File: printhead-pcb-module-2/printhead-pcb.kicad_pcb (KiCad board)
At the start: 2 copper layers, 136.4 x 35.3 mm, 55 parts, among them J1 Power, J13 Steckverbinder_Male_1, J14 Steckverbinder_Male_2, J15 Steckverbinder_Female_2, J2 Fan_12/5V_Regelung, J3 DATA, J4 FAN0, J5 FAN1, J6 FAN2, J7 FAN4, Q1 DTC143E, Q2 DTC143E, Q4 DTC143E, Q5 DTC143E, U1 PCA9615DP, U2 EMC2302-2-AIZL-TR, U5 PCA9536D, U6 AP7361C-33E

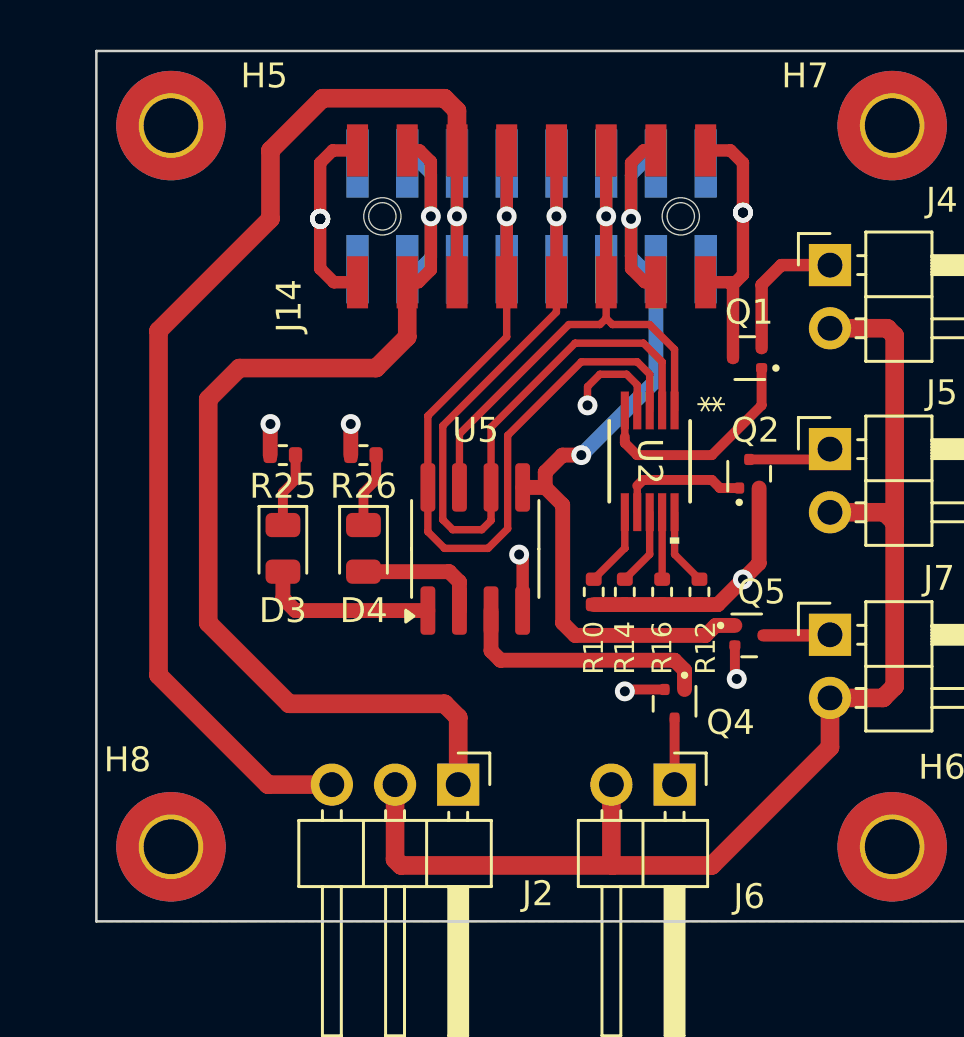
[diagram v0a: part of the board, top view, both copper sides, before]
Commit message: added documentation, fixed isolated copper fill warnings
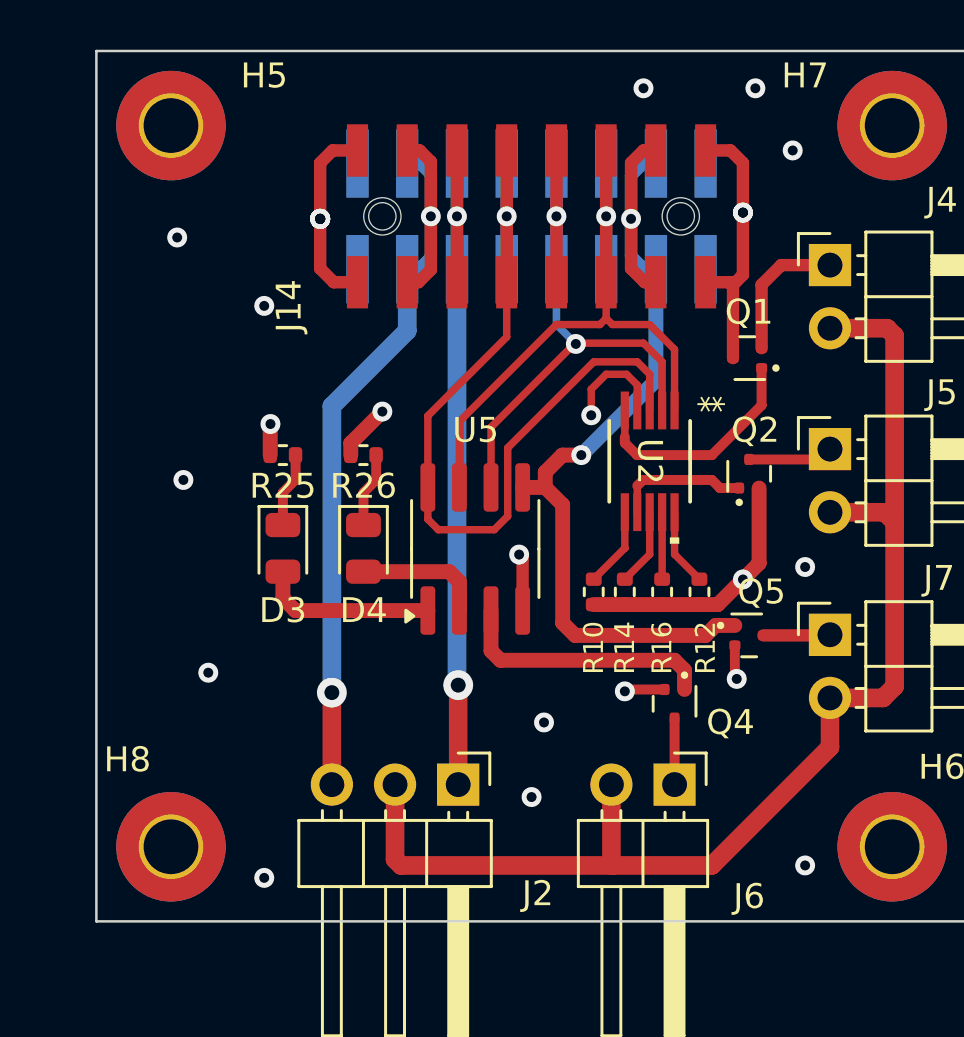
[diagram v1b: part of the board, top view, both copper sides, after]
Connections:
- J2 pad 1: +12V -> +5V
- J2 pad 3: +5V -> +12V
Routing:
- net +5V: track 129.4 -> 108.2 mm, vias 1 -> 2
- net +12V: track 78.4 -> 65.9 mm, vias 1 -> 2
- net SCL: track 60.3 -> 48.6 mm, vias 1 -> 2
- net +3V3: track 49.8 -> 48.3 mm
- net GND: track 41.0 -> 42.2 mm, vias 14 -> 26
- removed copper zone on F.Cu, net SCL

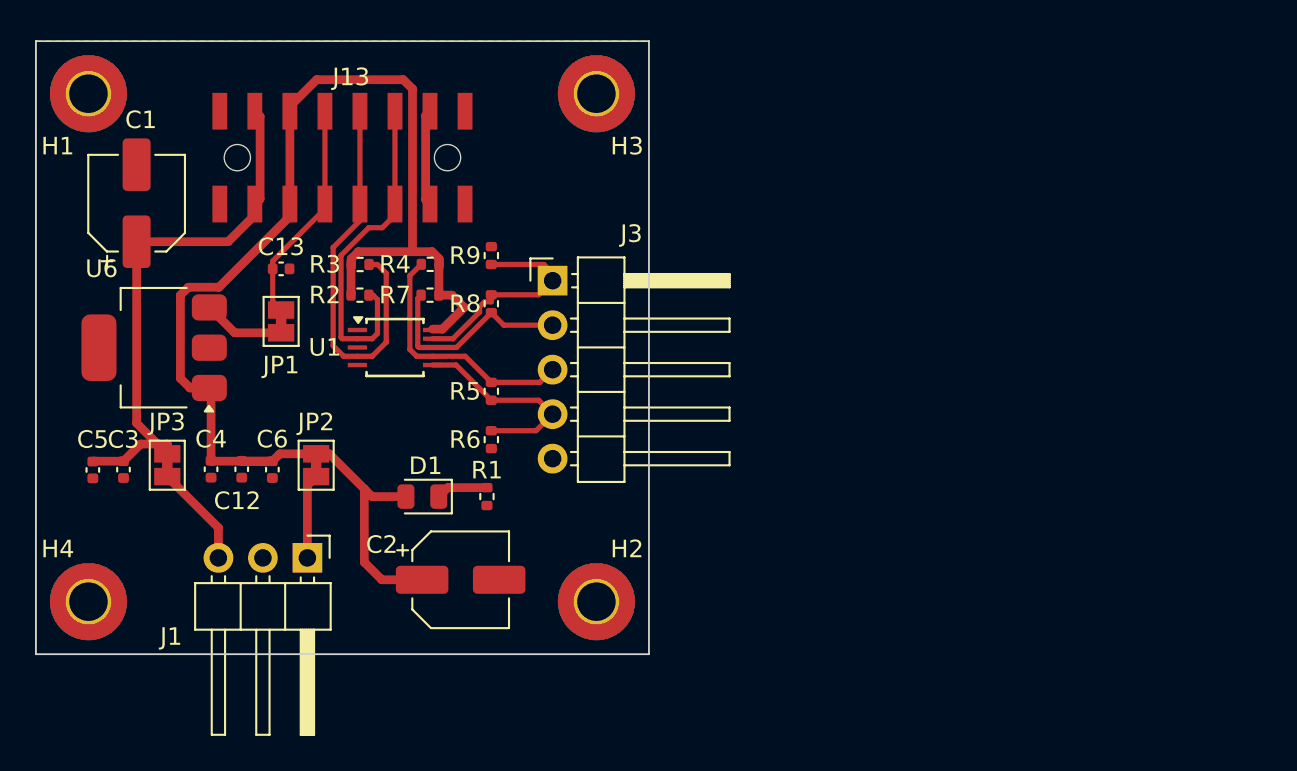
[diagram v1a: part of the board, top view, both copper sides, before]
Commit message: added first module into projet of second module
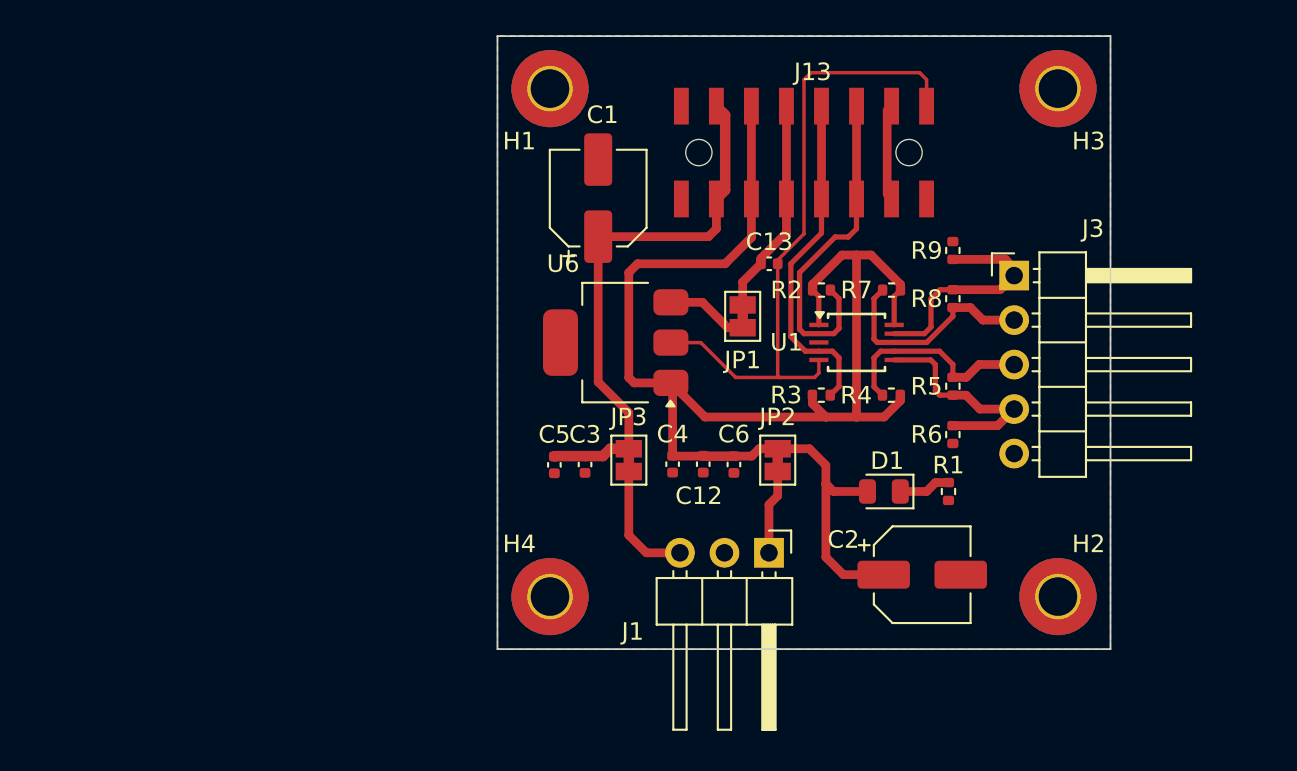
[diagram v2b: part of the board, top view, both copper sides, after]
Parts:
- moved C13 27.9 mm to (90.4, 113.0)
- moved R4 27.4 mm to (97.4, 120.5)
- moved R3 27.4 mm to (93.4, 120.5)
- moved C1 26.4 mm to (80.7, 109.3)
- moved C12 26.4 mm to (86.7, 124.5)
- moved C2 26.4 mm to (99.2, 130.8)
- moved C3 26.4 mm to (79.9, 124.5)
- moved C4 26.4 mm to (84.9, 124.5)
- moved C5 26.4 mm to (78.2, 124.5)
- moved C6 26.4 mm to (88.4, 124.5)
- moved D1 26.4 mm to (97.0, 126.0)
- moved H1 26.4 mm to (77.9, 103.0)
- moved H2 26.4 mm to (106.9, 132.0)
- moved H3 26.4 mm to (106.9, 103.0)
- moved H4 26.4 mm to (77.9, 132.0)
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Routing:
- net GND: track 42.2 -> 78.8 mm
- net +5V: track 108.2 -> 117.7 mm
- net SCL: track 48.6 -> 45.3 mm
- net DSCLP: track 14.4 -> 11.8 mm
- net Net-(J1-Pin_3): track 5.85 -> 6.97 mm
- net DSCLM: track 11.9 -> 12.8 mm
- net DSDAP: track 11.8 -> 12.5 mm
- net DSDAM: track 12.8 -> 13.3 mm
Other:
- board size 136.4 x 35.3 mm -> 110.1 x 35 mm

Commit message: finished third module
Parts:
- added C10: 0.1µF, Capacitor_SMD:C_0402_1005Metric, F.Cu at (175.0, 68.0)
- added C11: 0.1µF, Capacitor_SMD:C_0402_1005Metric, F.Cu at (175.0, 62.0)
- added C7: 0.1µF, Capacitor_SMD:C_0402_1005Metric, F.Cu at (172.5, 75.0)
- added C8: 0.1µF, Capacitor_SMD:C_0402_1005Metric, F.Cu at (170.3, 51.8)
- added C9: 0.1µF, Capacitor_SMD:C_0402_1005Metric, F.Cu at (175.0, 74.0)
- added D2: BLUE, LED_SMD:LED_0805_2012Metric, F.Cu at (167.0, 74.3)
- added H10: MountHole, MountingHole:MountingHole_2.2mm_M2_Pad_TopBottom, F.Cu at (182.0, 82.0)
- added H11: MountHole, MountingHole:MountingHole_2.2mm_M2_Pad_TopBottom, F.Cu at (182.0, 53.0)
- added H12: MountHole, MountingHole:MountingHole_2.2mm_M2_Pad_TopBottom, F.Cu at (153.0, 82.0)
- added H9: MountHole, MountingHole:MountingHole_2.2mm_M2_Pad_TopBottom, F.Cu at (153.0, 53.0)
- added J10: T2, Connector_PinHeader_2.54mm:PinHeader_1x02_P2.54mm_Horizontal, F.Cu at (179.5, 66.0)
- added J11: T3, Connector_PinHeader_2.54mm:PinHeader_1x02_P2.54mm_Horizontal, F.Cu at (179.5, 58.6)
- added J12: Breakout_Board_ADXL345, Connector_PinHeader_2.54mm:PinHeader_1x04_P2.54mm_Horizontal, F.Cu at (166.7, 79.5)
- added J16: Steckverbinder_Male_3, CustomFotLibByJan:BF100-16-A-D-1-0640-L-C, F.Cu at (160.5, 59.3)
- added J17: Steckverbinder_Female_3, CustomFotLibByJan:BF030-16A-B1-0360-0277-0600-LB, B.Cu at (174.5, 58.8)
- added J8: T0, Connector_PinHeader_2.54mm:PinHeader_1x02_P2.54mm_Horizontal, F.Cu at (175.5, 79.5)
- added J9: T1, Connector_PinHeader_2.54mm:PinHeader_1x02_P2.54mm_Horizontal, F.Cu at (179.5, 73.5)
- added R18: 4k7, Resistor_SMD:R_0402_1005Metric, F.Cu at (170.5, 75.0)
- added R19: 4k7, Resistor_SMD:R_0402_1005Metric, F.Cu at (175.0, 76.0)
- added R20: 330, Resistor_SMD:R_0402_1005Metric, F.Cu at (164.5, 75.1)
- added R21: 4k7, Resistor_SMD:R_0402_1005Metric, F.Cu at (175.0, 70.0)
- added R22: 4k7, Resistor_SMD:R_0402_1005Metric, F.Cu at (175.0, 64.0)
- added U4: ADS1015IDGS, Package_SO:TSSOP-10_3x3mm_P0.5mm, F.Cu at (168.8, 68.8)
- moved D4 70.7 mm to (110.7, 70.0)
- moved J2 70.7 mm to (114.5, 79.5)
- moved R26 70.7 mm to (110.7, 66.2)
- moved U5 70.7 mm to (115.2, 70.0)
- moved D3 70.7 mm to (107.5, 70.0)
- moved H5 70.7 mm to (103.0, 53.0)
- moved H6 70.7 mm to (132.0, 82.0)
- moved H7 70.7 mm to (132.0, 53.0)
- moved H8 70.7 mm to (103.0, 82.0)
- moved J14 70.7 mm to (110.5, 59.3)
- moved J15 70.7 mm to (124.5, 58.8)
- moved J4 70.7 mm to (129.5, 58.6)
- moved J5 70.7 mm to (129.5, 66.0)
- moved J6 70.7 mm to (123.2, 79.5)
- moved J7 70.7 mm to (129.5, 73.5)
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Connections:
- net +3V3 renamed AREF
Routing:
- net AREF: track 47.9 -> 105.2 mm, vias 1 -> 4
- net GND: track 78.8 -> 126.6 mm, vias 26 -> 28
- net SCL: track 45.3 -> 79.0 mm, vias 2 -> 3
- net SDA: track 46.4 -> 79.8 mm, vias 1 -> 2
- net +5V: track 117.7 -> 148.3 mm, vias 2 -> 4
- net ADC3: track 0.00 -> 12.7 mm
- net IO3: track 42.5 -> 54.9 mm, vias 2 -> 3
- net +12V: track 65.9 -> 78.1 mm, vias 2 -> 3
- net ADC1: track 0.00 -> 11.6 mm
- net ADC2: track 0.00 -> 11.1 mm
- net ADC0: track 0.00 -> 9.66 mm
- net Net-(D2-A): track 0.00 -> 3.57 mm
- net Net-(D2-K): track 0.00 -> 2.63 mm
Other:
- board size 110.1 x 35 mm -> 135 x 35 mm
